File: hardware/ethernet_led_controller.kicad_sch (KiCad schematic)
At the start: 31 parts, among them J1 WeMos_CH340G_USB_to_SERIAL, J10 Conn_01x02, J2 RJ45, J3 RJ45, J4 MP1584EN_5v_stepdown, J4 terminal_04, J5 terminal_04, J6 Barrel_Jack_Switch, J7 terminal_02, J9 Conn_01x03, Q1 2N3904, Q2 2N3904, SW1 SW_Push, U1 WT32-ETH01, U2 74HC245

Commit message: updating hardware for v1_1_0 - change layouts etc
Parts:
- removed J10: Conn_01x02, Connector_PinHeader_2.54mm:PinHeader_1x03_P2.54mm_Horizontal, symbol Connector_Generic:Conn_01x03
- removed J4: terminal_04, lib_fp:terminal_04, symbol Connector_Generic:Conn_01x04
- removed J7: terminal_02, lib_fp:terminal_02, symbol Connector_Generic:Conn_01x02
- removed J9: Conn_01x03, Connector_PinHeader_2.54mm:PinHeader_1x03_P2.54mm_Horizontal, symbol Connector_Generic:Conn_01x03
- added C3: 0.1u, Capacitor_THT:C_Disc_D6.0mm_W2.5mm_P5.00mm, symbol Device:C_Small
- J5: value terminal_04 -> terminal_08; footprint lib_fp:terminal_04 -> TerminalBlock_Phoenix:TerminalBlock_Phoenix_PT-1,5-8-3.5-H_1x08_P3.50mm_Horizontal; symbol Connector_Generic:Conn_01x04 -> Connector_Generic:Conn_01x08
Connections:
- net +5V: now also C3.1
- net GND: now also C3.2
- net at J2.5, R5.2: now also J5.3 (Pin_3)
- net at J1.3 (Pin_3): now also J6.3
- net at J3.1, R7.2: now also J5.5 (Pin_5); no longer J5.1 (Pin_1)
- net at J3.3, R8.2: now also J5.6 (Pin_6); no longer J5.2 (Pin_2)
- net at J3.5, R9.2: now also J5.7 (Pin_7); no longer J5.3 (Pin_3)
- net at J3.7, R10.2: now also J5.8 (Pin_8); no longer J5.4 (Pin_4)
- net at J2.1, R3.2: now also J5.1 (Pin_1)
- net at F1.2: now also J4.1 (Pin_1)
- net at J2.3, R4.2: now also J5.2 (Pin_2)
- net at J2.7, R6.2: now also J5.4 (Pin_4)
- no-connect marks 6 -> 4
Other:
- note removed: "+V"
- note removed: "12v/5v input voltage selection"
- note removed: "GND"
- note removed: "power over serial"

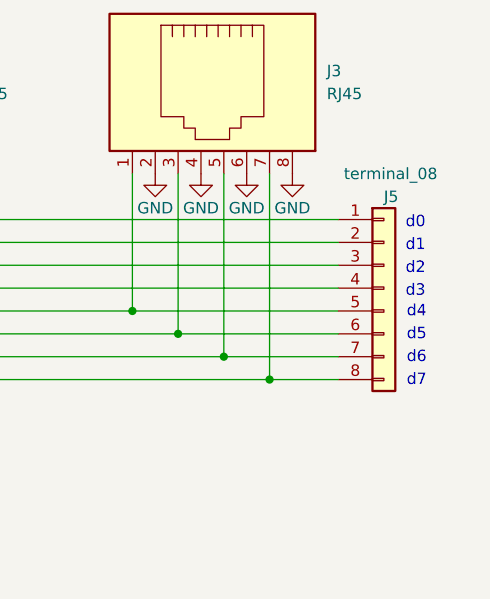
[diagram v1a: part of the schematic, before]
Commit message: updated board to use 4x terminal blocks
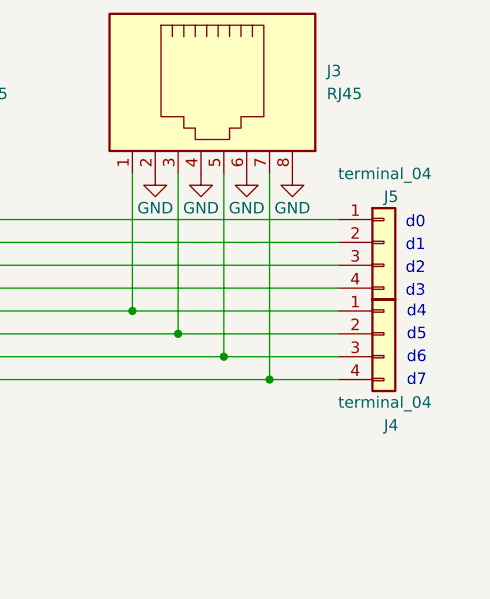
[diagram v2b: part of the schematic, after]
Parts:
- added J4: terminal_04, TerminalBlock_Phoenix:TerminalBlock_Phoenix_PT-1,5-4-3.5-H_1x04_P3.50mm_Horizontal, symbol Connector_Generic:Conn_01x04
- J5: value terminal_08 -> terminal_04; footprint TerminalBlock_Phoenix:TerminalBlock_Phoenix_PT-1,5-8-3.5-H_1x08_P3.50mm_Horizontal -> TerminalBlock_Phoenix:TerminalBlock_Phoenix_PT-1,5-4-3.5-H_1x04_P3.50mm_Horizontal; symbol Connector_Generic:Conn_01x08 -> Connector_Generic:Conn_01x04
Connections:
- net at J3.1, R7.2: now also J4.1 (Pin_1); no longer J5.5 (Pin_5)
- net at J3.3, R8.2: now also J4.2 (Pin_2); no longer J5.6 (Pin_6)
- net at J3.5, R9.2: now also J4.3 (Pin_3); no longer J5.7 (Pin_7)
- net at J3.7, R10.2: now also J4.4 (Pin_4); no longer J5.8 (Pin_8)
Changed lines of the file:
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@@
+    )
+  )
+  (symbol (lib_id "Connector_Generic:Conn_01x04") (at 256.54 147.32 0) (unit 1)
+    (in_bom yes) (on_board yes) (dnp no)
+    (property "Reference" "J4" (at 256.54 157.48 0)
+      (effects (font (size 1.27 1.27)) (justify left))
+    )
+    (property "Value" "terminal_04" (at 251.46 154.94 0)
+      (effects (font (size 1.27 1.27)) (justify left))
+    )
+    (property "Footprint" "TerminalBlock_Phoenix:TerminalBlock_Phoenix_PT-1,5-4-3.5-H_1x04_P3.50mm_Horizontal" (at 256.54 147.32 0)
+      (effects (font (size 1.27 1.27)) hide)
+    )
+    (property "Datasheet" "~" (at 256.54 147.32 0)
+      (effects (font (size 1.27 1.27)) hide)
+    )
+    (pin "2")
+    (pin "4")
+    (pin "1")
+    (pin "3")
+    (instances
+      (project "ethernet_led_controller"
+        (path "/44d13876-5634-4585-a15b-44faf5e7dd51"
+          (reference "J4") (unit 1)
+        )
+      )
     )
   )
@@
     )
   )
-  (symbol (lib_id "Connector_Generic:Conn_01x08") (at 256.54 142.24 0) (unit 1)
+  (symbol (lib_id "Connector_Generic:Conn_01x04") (at 256.54 137.16 0) (unit 1)
     (in_bom yes) (on_board yes) (dnp no)
     (property "Reference" "J5" (at 256.54 132.08 0)
       (effects (font (size 1.27 1.27)) (justify left))
     )
-    (property "Value" "terminal_08" (at 252.095 129.54 0)
-      (effects (font (size 1.27 1.27)) (justify left))
-    )
-    (property "Footprint" "TerminalBlock_Phoenix:TerminalBlock_Phoenix_PT-1,5-8-3.5-H_1x08_P3.50mm_Horizontal" (at 256.54 142.24 0)
-      (effects (font (size 1.27 1.27)) hide)
-    )
-    (property "Datasheet" "~" (at 256.54 142.24 0)
-      (effects (font (size 1.27 1.27)) hide)
-    )
-    (pin "2")
-    (pin "4")
-    (pin "1")
-    (pin "3")
-    (pin "7")
-    (pin "8")
-    (pin "5")
-    (pin "6")
-    (instances
-      (project "ethernet_led_controller"
+    (property "Value" "terminal_04" (at 251.46 129.54 0)
+      (effects (font (size 1.27 1.27)) (justify left))
+    )
+    (property "Footprint" "TerminalBlock_Phoenix:TerminalBlock_Phoenix_PT-1,5-4-3.5-H_1x04_P3.50mm_Horizontal" (at 256.54 137.16 0)
+      (effects (font (size 1.27 1.27)) hide)
+    )
+    (property "Datasheet" "~" (at 256.54 137.16 0)
+      (effects (font (size 1.27 1.27)) hide)
+    )
+    (pin "2")
+    (pin "4")
+    (pin "1")
+    (pin "3")
+    (instances
+      (project "ethernet_led_controller"

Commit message: update hardware to v1_2_0
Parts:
- added D2: 1n5819, Diode_THT:D_DO-34_SOD68_P7.62mm_Horizontal, symbol Device:D_Small
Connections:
- net +5V: now also D2.1 (K)
- net at J1.3 (Pin_3): now also D2.2 (A); no longer J6.3
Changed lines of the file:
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@@
-    (stroke (width 0) (type default))
-  )
-  (wire (pts (xy 50.8 63.5) (xy 50.8 170.18))
     (stroke (width 0) (type default))
   )
@@
     (stroke (width 0) (type default))
   )
-  (wire (pts (xy 50.8 170.18) (xy 27.94 170.18))
-    (stroke (width 0) (type default))
-  )
   (wire (pts (xy 63.5 35.56) (xy 45.72 35.56))
     (stroke (width 0) (type default))
@@
   )
   (wire (pts (xy 147.32 107.95) (xy 147.32 130.81))
+    (stroke (width 0) (type default))
+  )
+  (wire (pts (xy 50.8 55.88) (xy 50.8 63.5))
     (stroke (width 0) (type default))
   )
@@
         (path "/44d13876-5634-4585-a15b-44faf5e7dd51"
           (reference "#PWR011") (unit 1)
+        )
+      )
+    )
+  )
+  (symbol (lib_id "power:+5V") (at 50.8 50.8 0) (unit 1)
+    (in_bom yes) (on_board yes) (dnp no)
+    (property "Reference" "#PWR023" (at 50.8 54.61 0)
+      (effects (font (size 1.27 1.27)) hide)
+    )
+    (property "Value" "+5V" (at 48.26 48.26 0)
+      (effects (font (size 1.27 1.27)))
+    )
+    (property "Footprint" "" (at 50.8 50.8 0)
+      (effects (font (size 1.27 1.27)) hide)
+    )
+    (property "Datasheet" "" (at 50.8 50.8 0)
+      (effects (font (size 1.27 1.27)) hide)
+    )
+    (pin "1")
+    (instances
+      (project "ethernet_led_controller"
+        (path "/44d13876-5634-4585-a15b-44faf5e7dd51"
+          (reference "#PWR023") (unit 1)
         )
       )
@@
         )
       )
+    )
+  )
+  (symbol (lib_id "Device:D_Small") (at 50.8 53.34 270) (unit 1)
+    (in_bom yes) (on_board yes) (dnp no) (fields_autoplaced)
+    (property "Reference" "D2" (at 53.34 52.07 90)
+      (effects (font (size 1.27 1.27)) (justify left))
+    )
+    (property "Value" "1n5819" (at 53.34 54.61 90)
+      (effects (font (size 1.27 1.27)) (justify left))
+    )
+    (property "Footprint" "Diode_THT:D_DO-34_SOD68_P7.62mm_Horizontal" (at 50.8 53.34 90)
+      (effects (font (size 1.27 1.27)) hide)
+    )
+    (property "Datasheet" "~" (at 50.8 53.34 90)
+      (effects (font (size 1.27 1.27)) hide)
+    )
+    (property "Sim.Device" "D" (at 50.8 53.34 0)
+      (effects (font (size 1.27 1.27)) hide)
+    )
+    (property "Sim.Pins" "1=K 2=A" (at 50.8 53.34 0)
+      (effects (font (size 1.27 1.27)) hide)
+    )
+    (pin "2")
+    (pin "1")
+    (instances
+      (project "ethernet_led_controller"
+        (path "/44d13876-5634-4585-a15b-44faf5e7dd51"
+          (reference "D2") (unit 1)
+        )
+      )
